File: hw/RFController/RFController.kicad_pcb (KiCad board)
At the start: 2 copper layers, 28.3 x 12.3 mm, 19 parts, among them J1 Conn_01x07, J2 Conn_01x01, SW1 SW_Push, U1 ADC128D818, Y1 Crystal

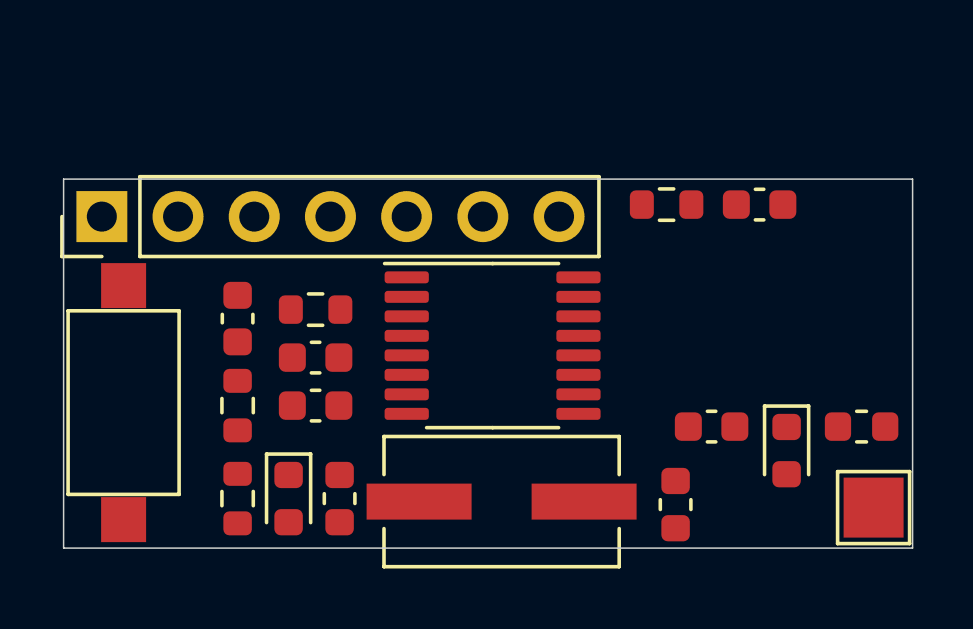
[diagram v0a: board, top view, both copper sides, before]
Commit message: rf controller added crystal 3d model
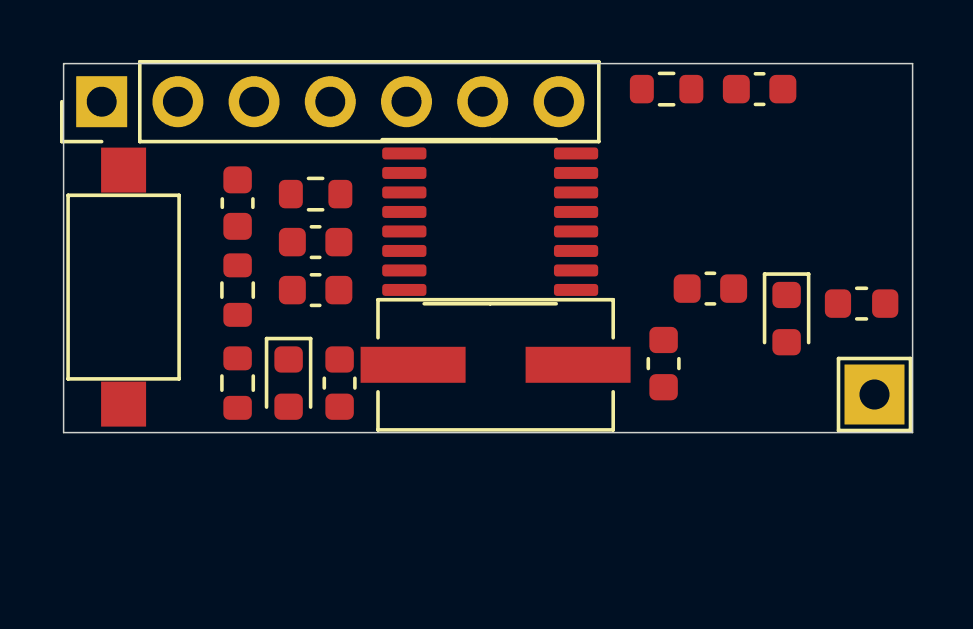
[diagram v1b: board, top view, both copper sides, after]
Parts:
- moved L2 4.72 mm to (150.0, 100.0)
- moved C5 4.60 mm to (151.6, 97.5)
- moved Y1 4.56 mm to (144.4, 100.0)
- moved D2 4.40 mm to (154.1, 98.5)
- moved U1 4.13 mm to (144.2, 95.3)
- moved L1 4.10 mm to (156.6, 98.0)
- moved C2 3.85 mm to (138.4, 97.5)
- moved C4 3.85 mm to (153.2, 90.8)
- moved R2 3.85 mm to (138.4, 94.3)
- moved R4 3.85 mm to (150.1, 90.8)
- moved R5 3.85 mm to (135.8, 97.5)
- moved C1 3.85 mm to (138.4, 96.0)
- moved C3 3.85 mm to (135.8, 94.7)
- moved D1 3.85 mm to (137.5, 100.7)
- moved L3 3.85 mm to (139.2, 100.7)
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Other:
- copper layers 2 -> 11
